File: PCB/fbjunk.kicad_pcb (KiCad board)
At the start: 2 copper layers, 31.6 x 22.9 mm, 3 parts

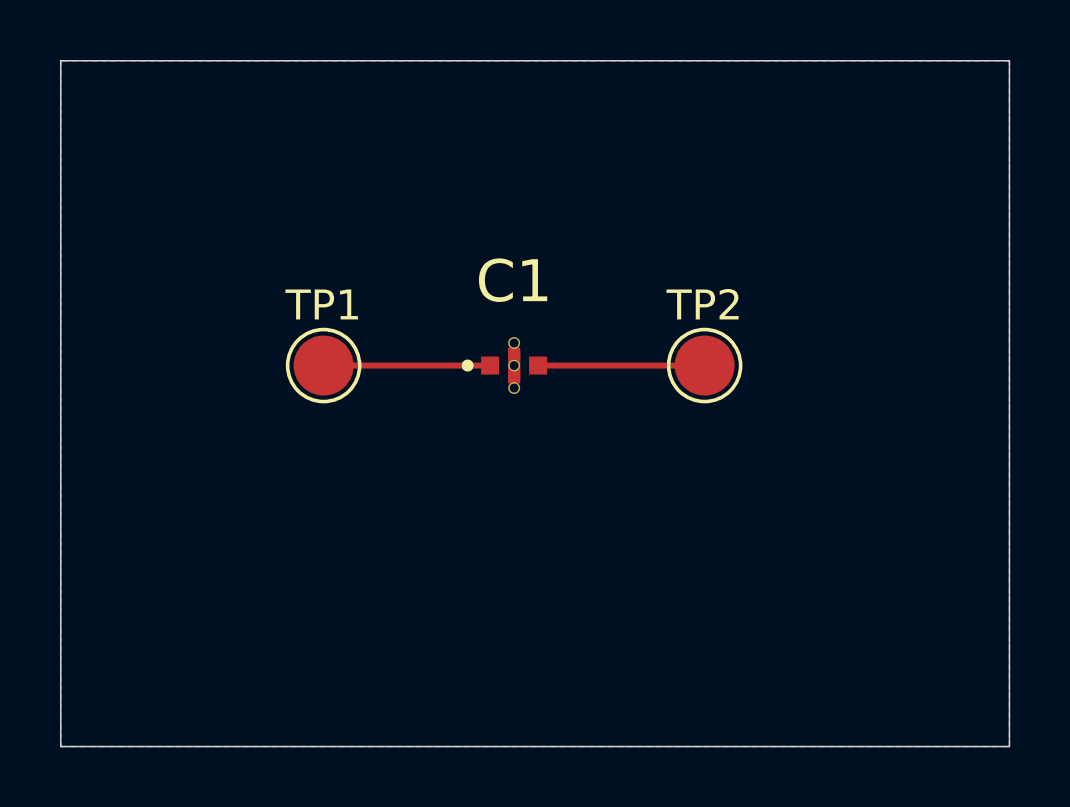
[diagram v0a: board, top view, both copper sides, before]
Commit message: fix footprint pin 2
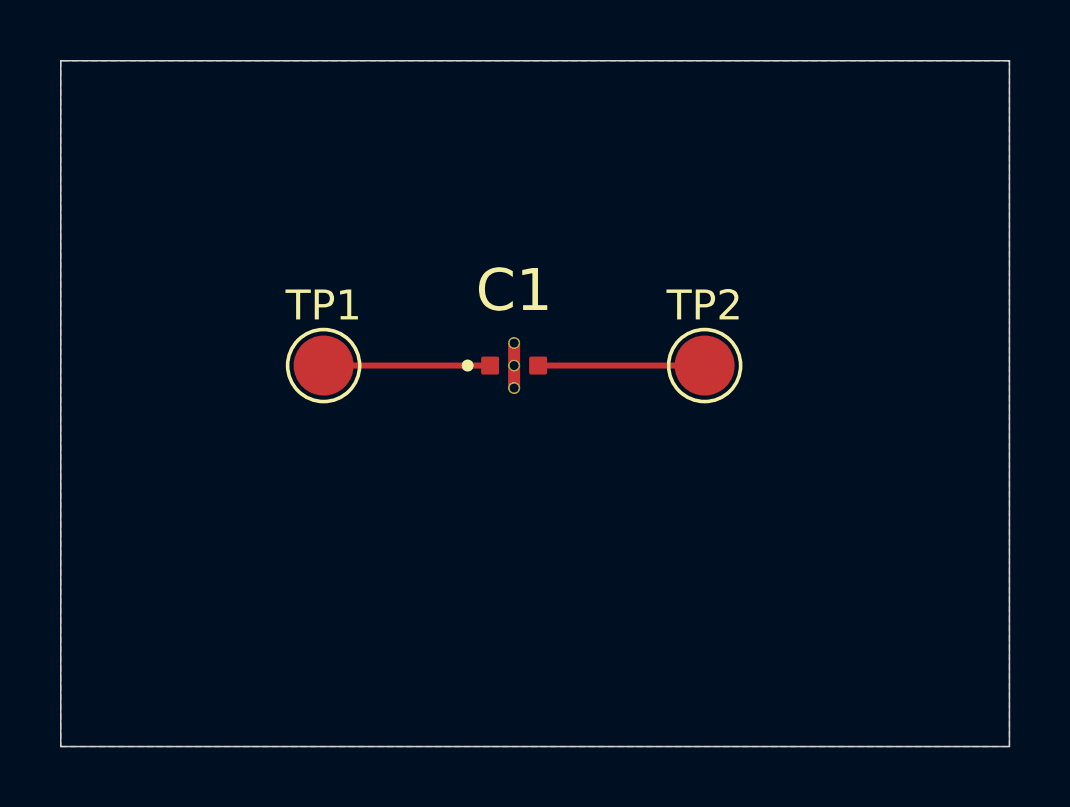
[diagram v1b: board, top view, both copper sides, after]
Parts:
- C1: footprint 000_LOCAL:FIL_NFM18CC101R1C3D -> 000_LOCAL:FIL_NFM18CC101R1C3D_modified

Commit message: add hack inverted pinout symbol
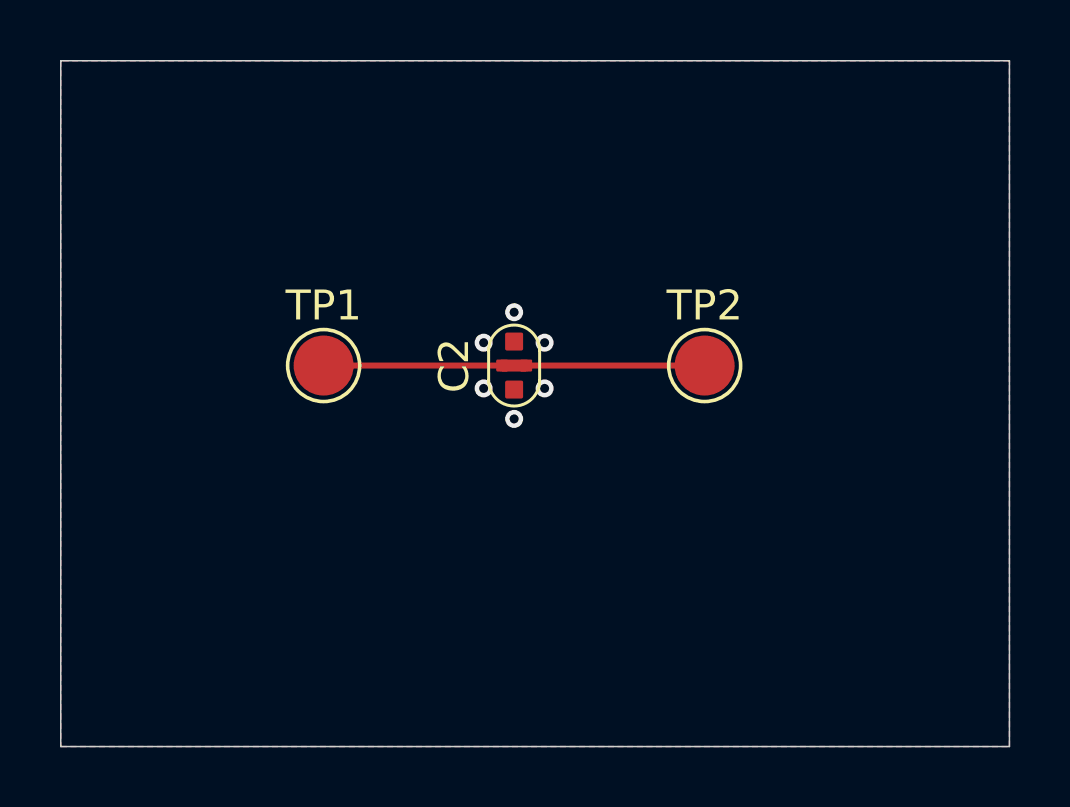
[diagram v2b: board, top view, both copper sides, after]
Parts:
- removed C1: C_Feedthrough, 000_LOCAL:FIL_NFM18CC101R1C3D_modified
- added C2: C_Feedthrough_CUSTOM_HACK, 000_LOCAL:C_0603_FeedThrough, F.Cu at (142.2, 99.1)
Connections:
- TP2 pad 1: Net-(C1-Pad3) -> +12V
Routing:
- net +12V: track 5.55 -> 12.7 mm
- net Net-(C1-Pad3): track 5.55 -> 0.00 mm
- net GND: vias 0 -> 6
